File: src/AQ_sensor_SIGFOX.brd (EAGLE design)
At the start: 110 x 64 mm, 35 parts, among them J1 F-1X03-SIP-100-32, SW1 PCM12SMTR, SW2 PCM12SMTR, U3 TEXAS_INSTRUMENTS_LM1117IMP-3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, X1 53048-08

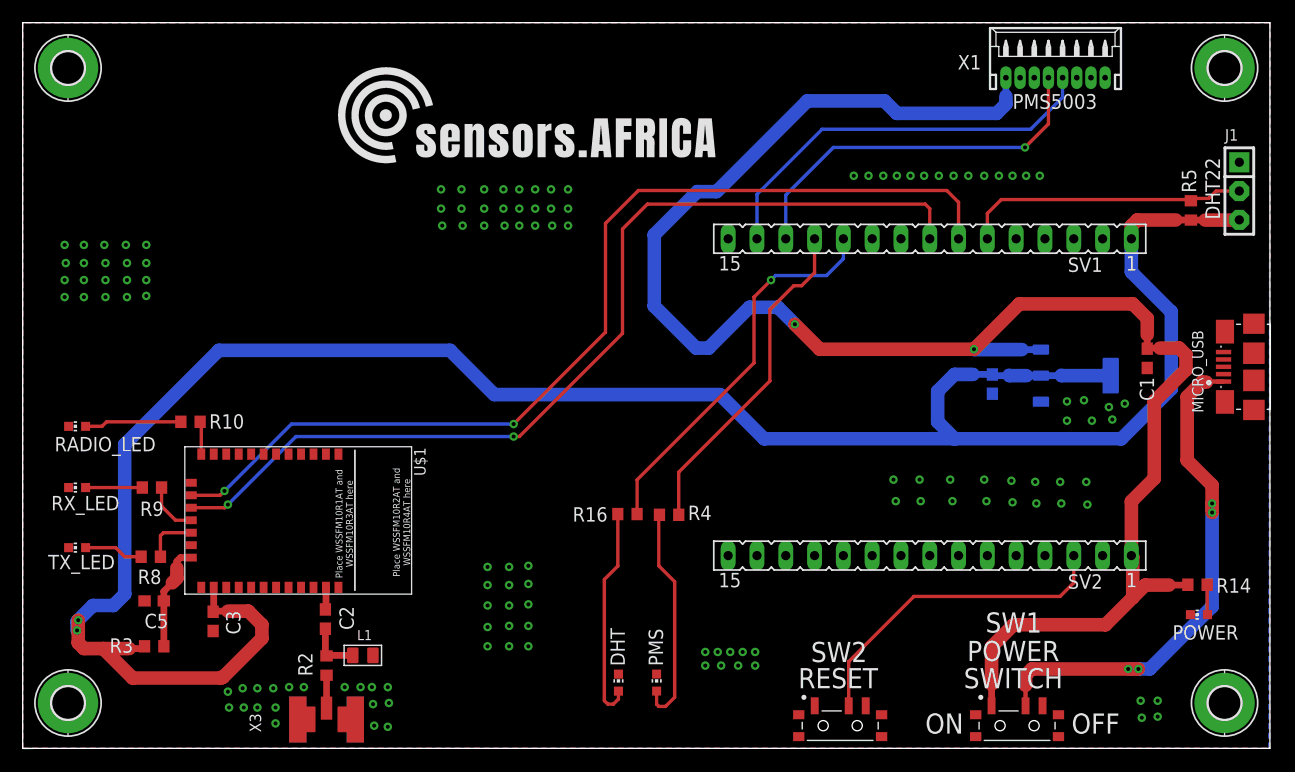
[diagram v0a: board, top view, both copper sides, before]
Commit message: fixed DRC warnings
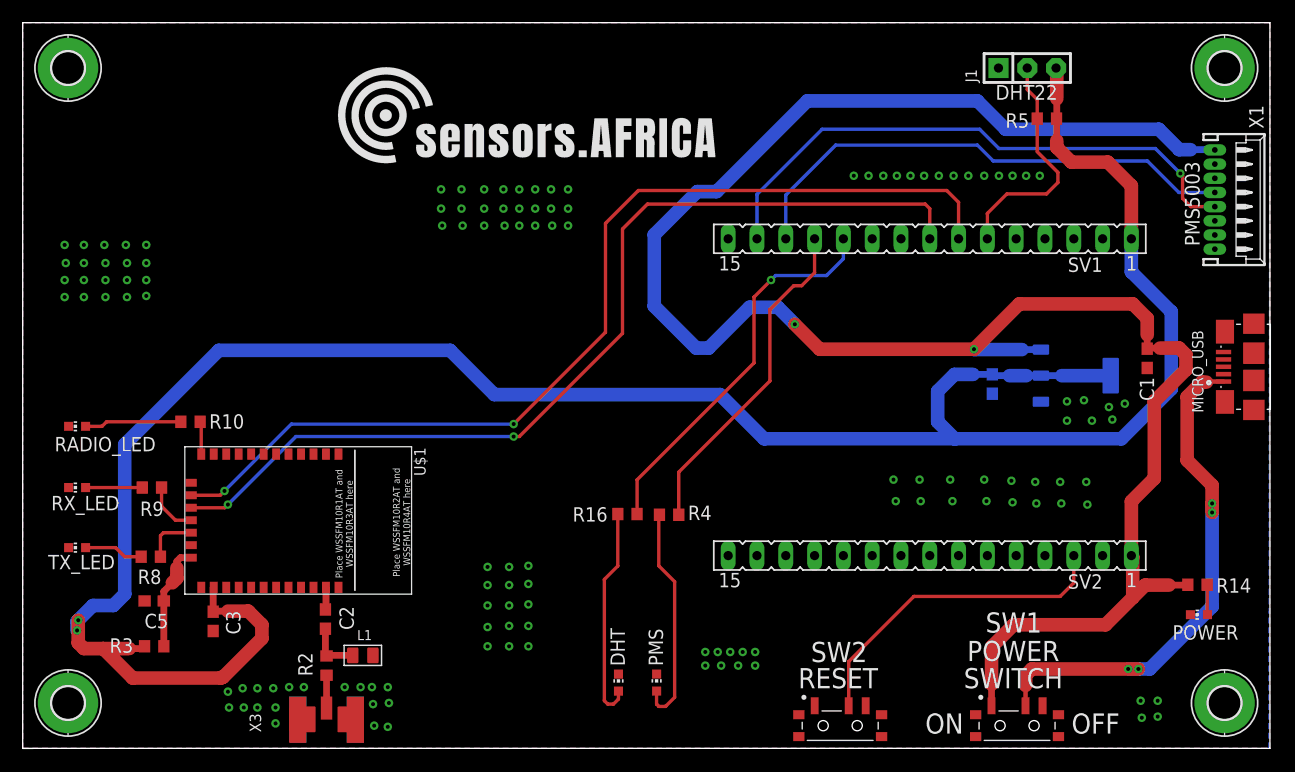
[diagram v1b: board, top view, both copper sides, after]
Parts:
- moved J1 21.6 mm to (88.6, 60.0), turned to 0 degrees
- moved X1 19.4 mm to (106.4, 48.4), turned to 270 degrees
- moved R5 15.1 mm to (90.3, 55.5), turned to 180 degrees
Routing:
- net +5V: track 156.6 -> 173.1 mm
- net PMS_TX: track 36.2 -> 50.7 mm, vias 0 -> 1
- net PMS_RX: track 33.7 -> 45.3 mm, vias 1 -> 0
- net +3V3: track 199.8 -> 208.0 mm
- net DHT_OUT: track 25.8 -> 20.8 mm
